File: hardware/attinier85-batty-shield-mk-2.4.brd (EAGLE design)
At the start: 36 x 25 mm, 8 parts, among them U1 ATTINIEST85_SHIELDV2

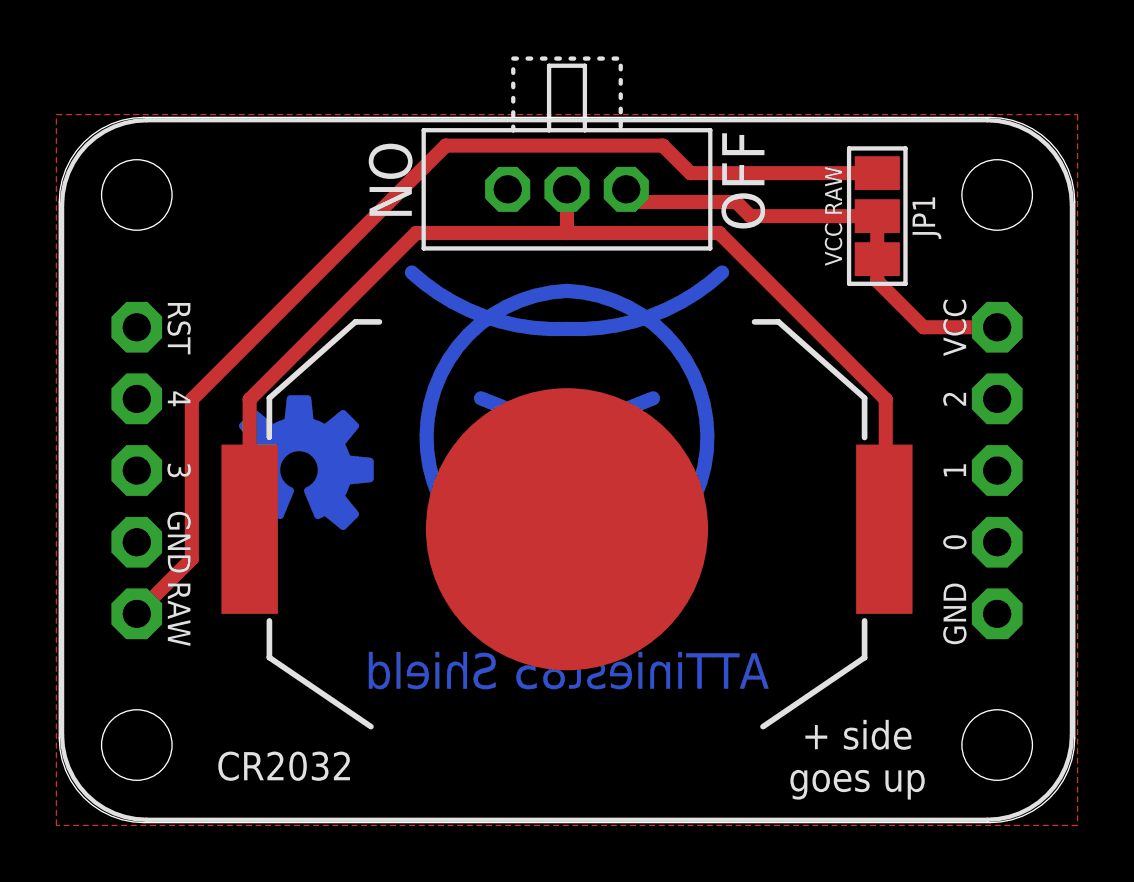
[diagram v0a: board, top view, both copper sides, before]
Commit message: renaming parts
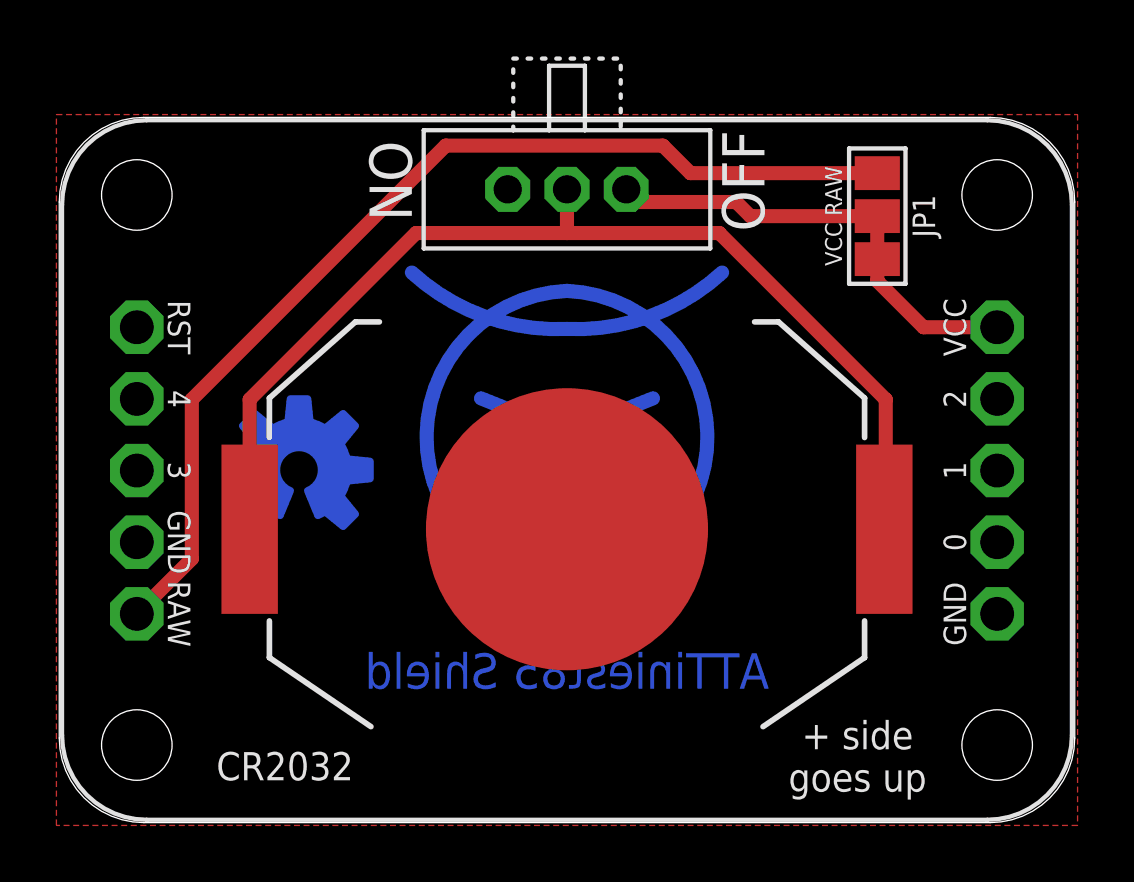
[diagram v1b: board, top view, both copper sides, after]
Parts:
- U1: value ATTINIEST85_SHIELDV2 -> ATTINIER85_SHIELDV2; device A_butts:ATTINIEST85_SHIELD_V2 -> A_butts:ATTINIER85_SHIELD_V2
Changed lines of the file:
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@@
 <setting verticaltext="up"/>
 </settings>
-<grid distance="0.1" unitdist="mm" unit="mm" style="lines" multiple="2" display="yes" altdistance="1" altunitdist="mil" altunit="mil"/>
+<grid distance="0.5" unitdist="mm" unit="mm" style="lines" multiple="2" display="yes" altdistance="1" altunitdist="mil" altunit="mil"/>
 <layers>
 <layer number="1" name="Top" color="4" fill="1" visible="yes" active="yes"/>
@@
 <attribute name="DESIGNER" value="Nobody" x="13.97" y="-1.27" size="1.778" layer="27" display="off"/>
 </element>
-<element name="U1" library="A_butts" package="ATTINIEST85_SHIELD_V2" value="ATTINIEST85_SHIELDV2" x="18" y="12.5"/>
+<element name="U1" library="A_butts" package="ATTINIER85_SHIELD_V2" value="ATTINIER85_SHIELDV2" x="18" y="12.5"/>
 <element name="BATT" library="A_butts" package="BATTCON_20MM_MINE" value="CR2032" x="18" y="10.4" smashed="yes" rot="R270">
 <attribute name="VALUE" x="8" y="2" size="1" layer="21" font="vector" ratio="12" rot="R180" align="center"/>
